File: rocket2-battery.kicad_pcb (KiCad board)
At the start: 4 copper layers, 91.4 x 69.8 mm, 141 parts, among them J1 Conn_01x07, J2 SMA, J3 ARM Cortex Debug, P1 PAD_SMD, P2 PAD_SMD, P3 PAD_SMD, P5 PAD_SMD, P6 PAD_SMD, P7 PAD_SMD, Q1 NMOS, Q2 NMOS, Q3 PMOS, Q4 PMOS, Q5 NMOS, Q6 NMOS, Q7 PMOS, Q8 PMOS, U1 3V3 LDO, Y1 16MHz

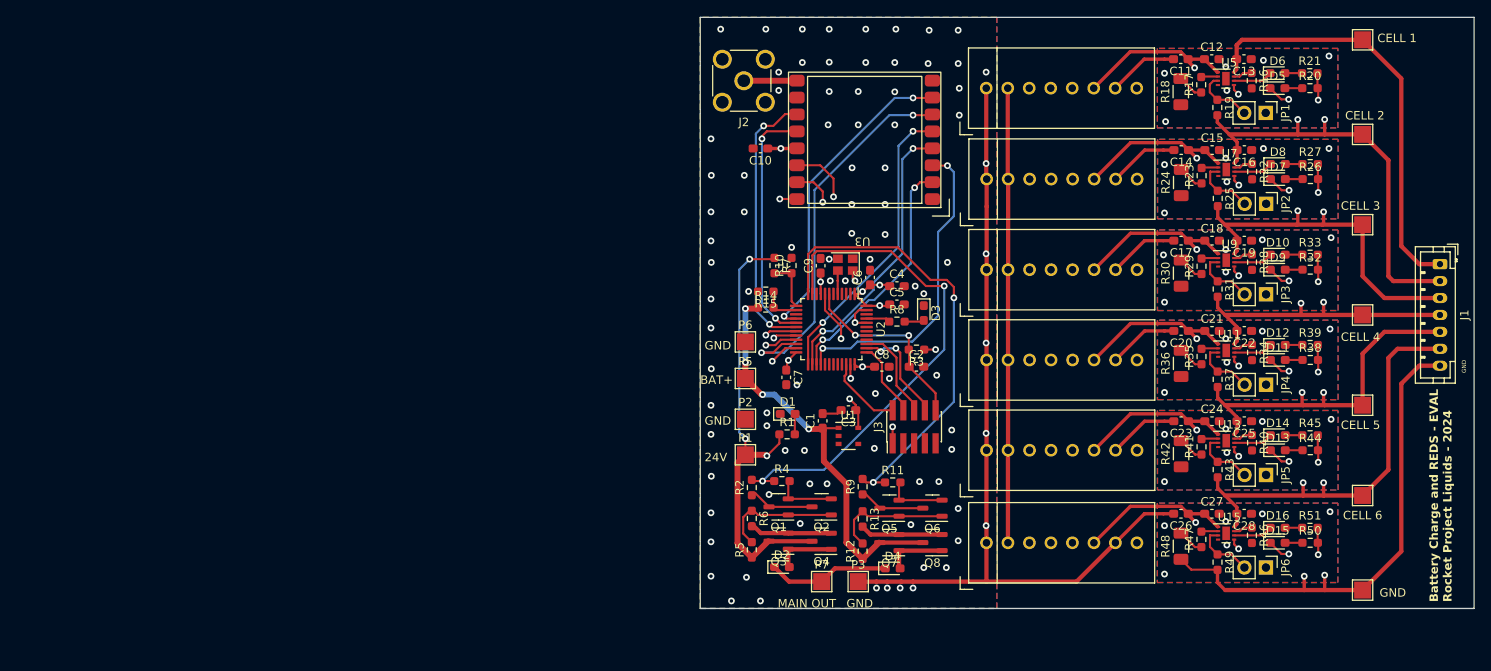
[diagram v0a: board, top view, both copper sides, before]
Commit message: Changed PMOS
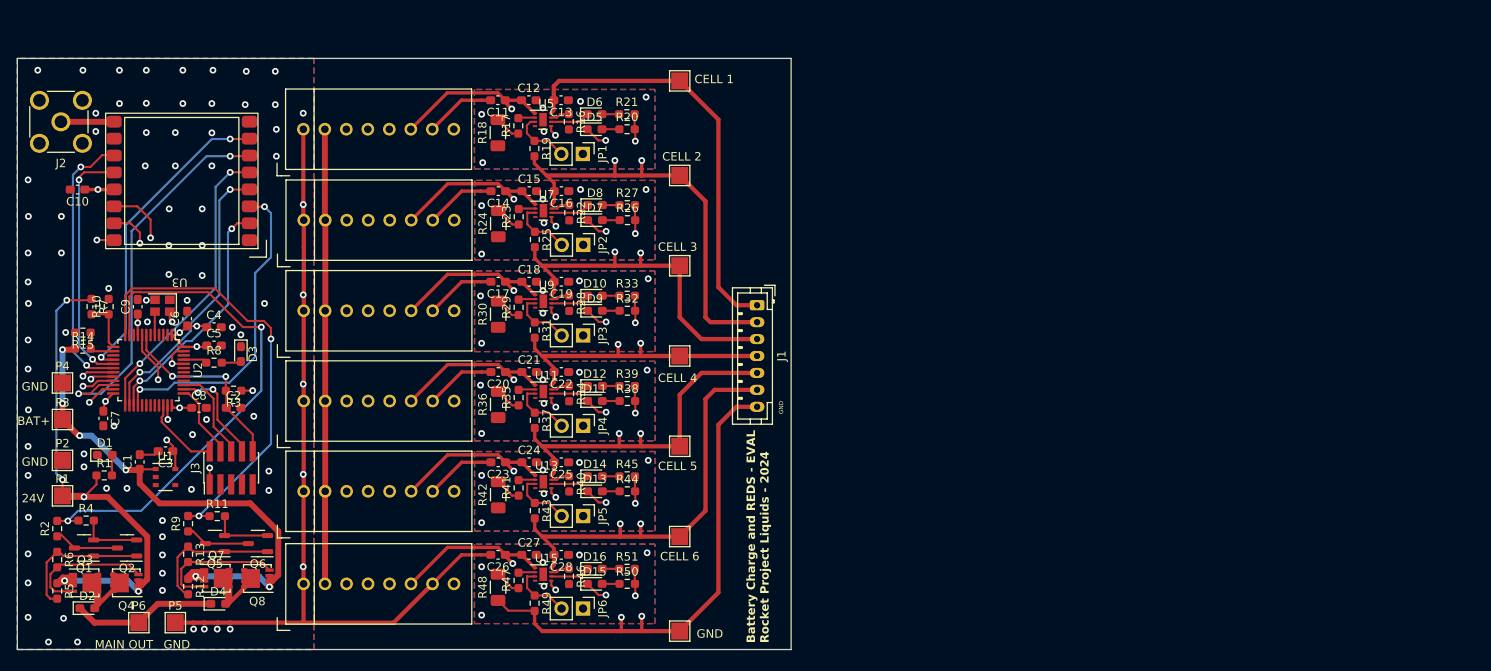
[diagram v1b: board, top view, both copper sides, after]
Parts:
- Q3, Q4, Q7, Q8: footprint Package_TO_SOT_SMD:SOT-23-3 -> Package_SO:Vishay_PowerPAK_1212-8_Single
- moved R4 82.4 mm to (111.6, 115.3)
- moved Q4 82.3 mm to (116.3, 122.7)
- moved D2 82.2 mm to (111.7, 125.7)
- moved Q2 82.2 mm to (116.4, 118.6)
- moved R2 82.2 mm to (108.2, 116.3)
- moved R5 82.2 mm to (108.2, 123.7), turned to -90 degrees
- moved R6 82.2 mm to (108.2, 120.0)
- moved Q1 82.2 mm to (111.3, 118.6)
- moved Q3 82.1 mm to (111.5, 122.7), turned to 0 degrees
- moved R21 80.8 mm to (175.5, 67.3)
- moved R27 80.8 mm to (175.5, 78.1)
- moved C10 80.8 mm to (110.6, 76.2)
- moved C11 80.8 mm to (160.2, 65.7)
- moved C12 80.8 mm to (163.9, 65.7)
- moved C13 80.8 mm to (167.7, 65.7)
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- renumbered P5 to P3, P6 to P4, P3 to P5, P7 to P6
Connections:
- Q3 pad 1: Net-(D2-A) -> +24V
- Q3 pad 2: Net-(Q3-G) -> +24V
- Q4 pad 1: Net-(D2-A) -> +24V
- Q4 pad 2: Net-(Q3-G) -> +24V
- Q7 pad 1: Net-(D4-A) -> /BATT_MAIN+
- Q7 pad 2: Net-(Q7-G) -> /BATT_MAIN+
- Q8 pad 1: Net-(D4-A) -> /BATT_MAIN+
- Q8 pad 2: Net-(Q7-G) -> /BATT_MAIN+
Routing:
- net /BATT_MAIN+: track 48.7 -> 65.6 mm, vias 4 -> 6
- net +24V: track 137.0 -> 149.2 mm, vias 3 -> 5
- net Net-(Q7-G): track 9.77 -> 15.8 mm
- net Net-(Q3-G): track 9.84 -> 15.8 mm
- net Net-(D2-A): track 7.24 -> 12.7 mm
- net Net-(D4-A): track 7.23 -> 12.6 mm
- net /MAIN+: track 15.0 -> 17.6 mm
- net Net-(Q1-D): track 14.0 -> 16.2 mm
- net Net-(Q5-D): track 14.3 -> 16.5 mm
- net MOSFET1: track 60.3 -> 61.5 mm
- net MOSFET2: track 54.0 -> 53.0 mm
- net GND: track 192.7 -> 192.6 mm, vias 102 -> 96

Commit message: some minor fixes
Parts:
- added D17: 30V 2A, Diode_SMD:D_0603_1608Metric_Pad1.05x0.95mm_HandSolder, F.Cu at (116.6, 109.1)
- added D18: 30V 2A, Diode_SMD:D_0603_1608Metric_Pad1.05x0.95mm_HandSolder, F.Cu at (117.5, 111.9)
- moved C1 0.89 mm to (118.5, 109.1)
- moved C3 0.89 mm to (121.5, 107.8)
- moved U1 0.89 mm to (121.5, 110.9)
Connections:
- C1 pad 1: /BATT_MAIN+ -> Net-(D17-K)
- U1 pad 1: /BATT_MAIN+ -> Net-(D17-K)
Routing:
- net Net-(D17-K): track 0.00 -> 5.80 mm
- net /BATT_MAIN+: track 65.6 -> 62.4 mm, vias 6 -> 7
- net +24V: track 149.2 -> 152.0 mm
- net GND: track 192.6 -> 190.9 mm, vias 96 -> 99
- net +3.3V: track 29.0 -> 27.3 mm

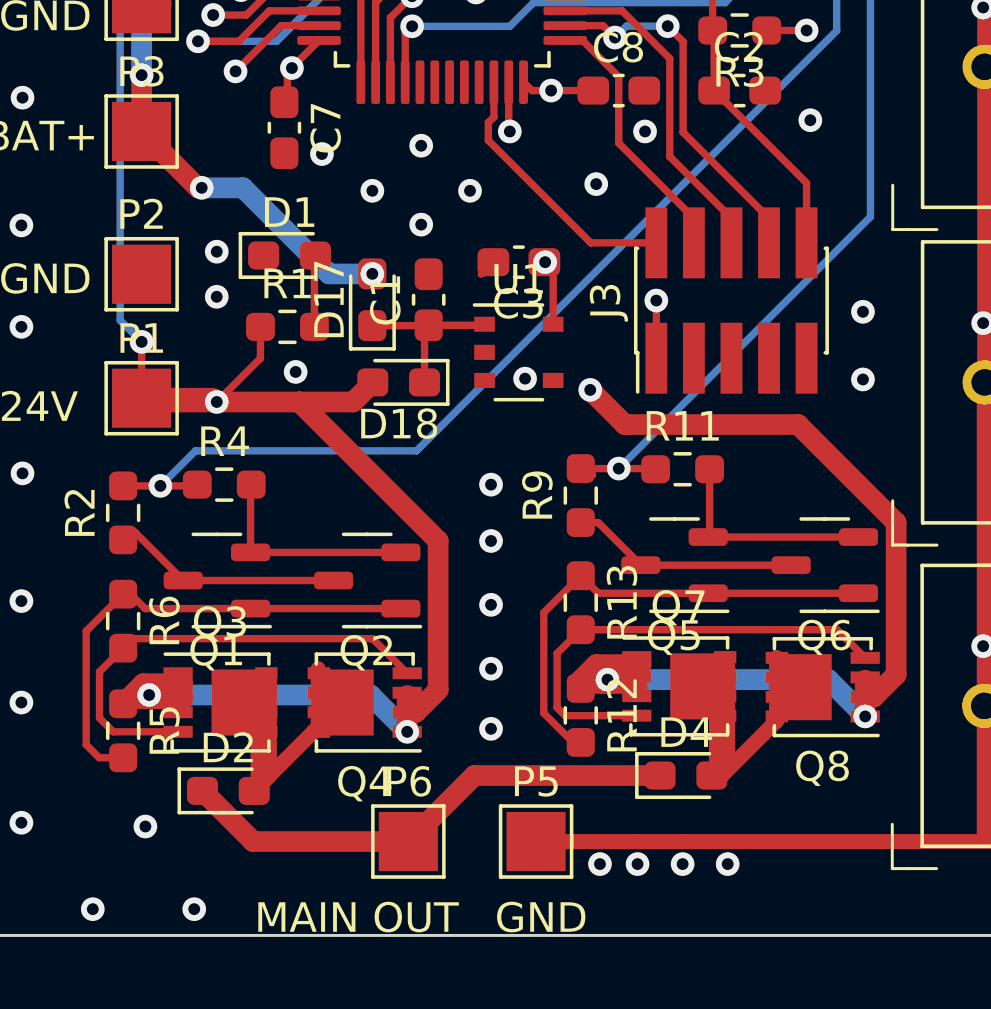
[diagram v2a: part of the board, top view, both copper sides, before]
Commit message: Fix diode footprints & other things I don't remember
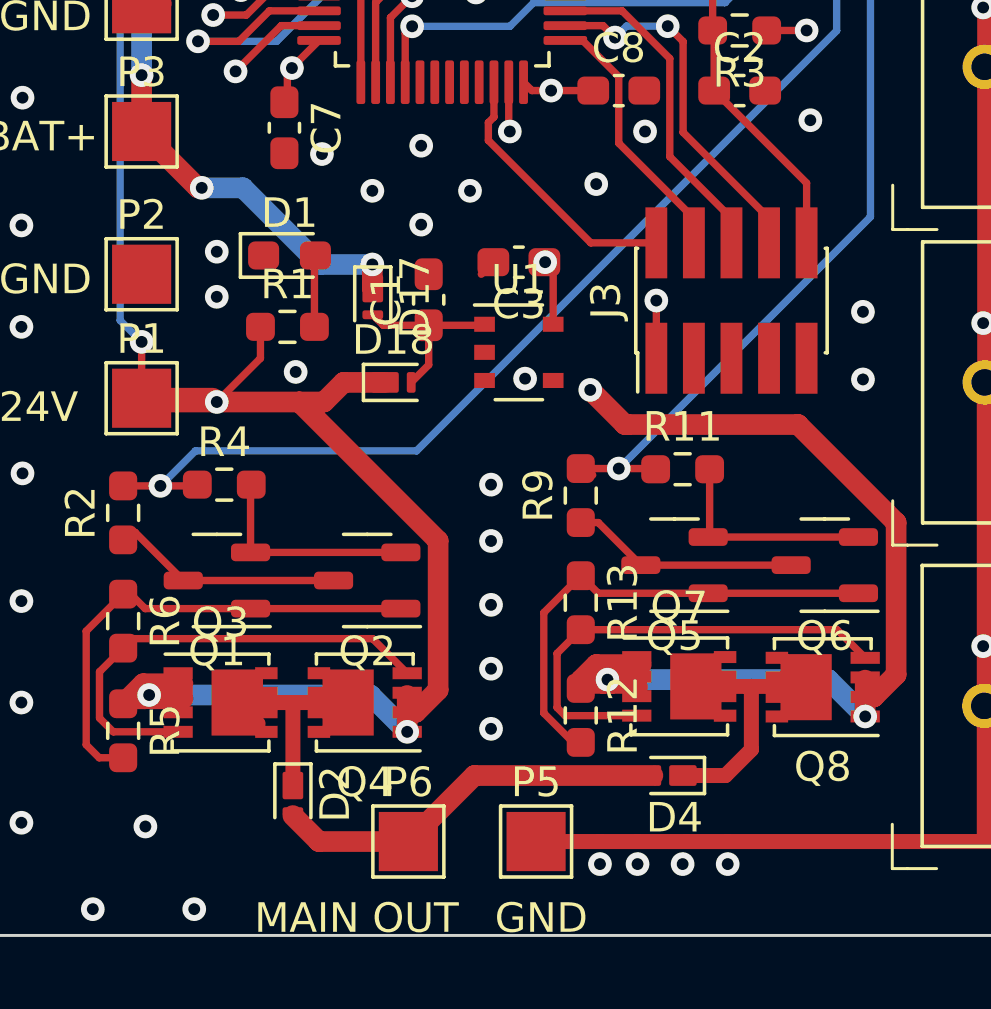
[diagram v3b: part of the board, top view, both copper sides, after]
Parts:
- D17, D18, D2, D4: footprint Diode_SMD:D_0603_1608Metric_Pad1.05x0.95mm_HandSolder -> Diode_SMD:Nexperia_DSN1608-2_1.6x0.8mm
- moved D2 2.18 mm to (113.9, 125.8), turned to -90 degrees
- moved D4 0.39 mm to (126.8, 125.2), turned to 180 degrees
- moved D18 0.17 mm to (117.3, 111.9), turned to 0 degrees
- moved D17 0.09 mm to (116.6, 109.0), turned to -90 degrees
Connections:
- D17 pad 1: Net-(D17-K) -> /BATT_MAIN+
- D17 pad 2: /BATT_MAIN+ -> Net-(D17-K)
- D18 pad 1: Net-(D17-K) -> +24V
- D18 pad 2: +24V -> Net-(D17-K)
- D2 pad 1: /MAIN+ -> Net-(D2-A)
- D2 pad 2: Net-(D2-A) -> /MAIN+
- D4 pad 1: /MAIN+ -> Net-(D4-A)
- D4 pad 2: Net-(D4-A) -> /MAIN+
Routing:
- net Net-(D2-A): track 12.7 -> 7.57 mm
- net /MAIN+: track 17.6 -> 13.5 mm
- net Net-(D4-A): track 12.6 -> 8.56 mm
- net /BATT_MAIN+: track 62.4 -> 63.2 mm
- net Net-(D17-K): track 5.80 -> 6.33 mm

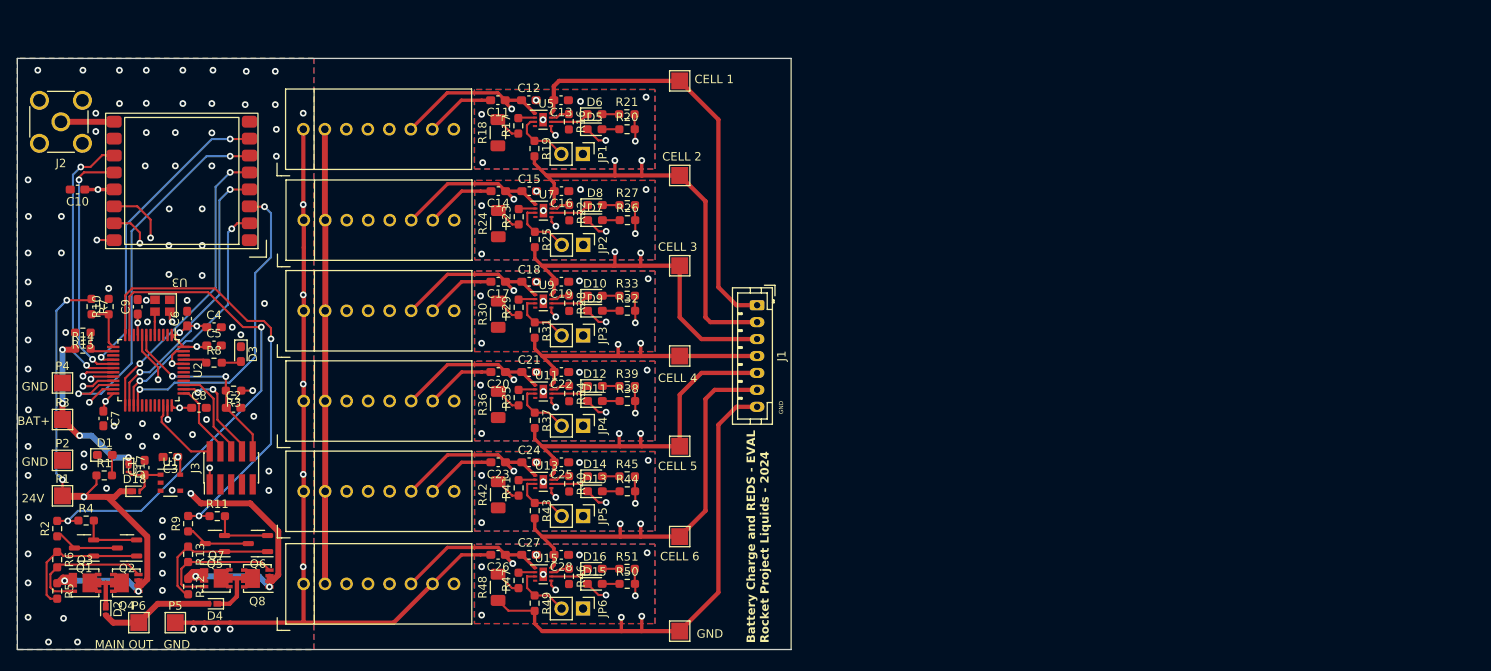
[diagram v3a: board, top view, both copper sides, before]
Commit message: fixed nmos
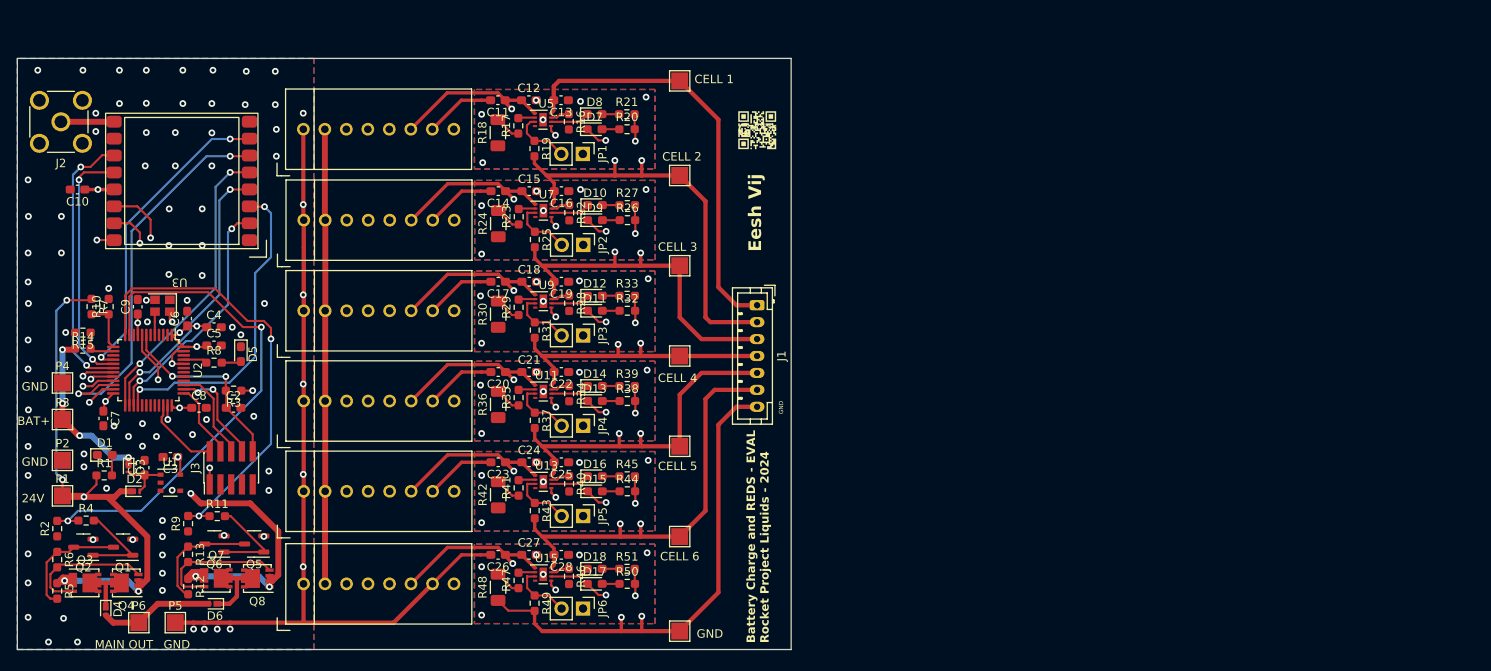
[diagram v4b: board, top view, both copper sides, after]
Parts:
- added G***: LOGO, LOGO, F.Cu at (190.9, 69.2)
- Q1, Q2, Q5, Q6: value NMOS -> Q_NMOS_GSD
- moved Q2 5.16 mm to (111.3, 118.5)
- moved Q6 5.14 mm to (126.7, 118.1)
- moved Q5 4.64 mm to (131.4, 118.1)
- moved Q1 4.62 mm to (116.0, 118.5)
- renumbered D8 to D10, D9 to D11, D10 to D12, D11 to D13, D12 to D14, D13 to D15, D14 to D16, D15 to D17, D16 to D18, D18 to D2, D17 to D3, D2 to D4, D3 to D5, D4 to D6, D5 to D7, D6 to D8, D7 to D9
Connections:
- Q1 pad 1: Net-(Q1-D) -> Net-(Q1-G)
- Q1 pad 2: Net-(Q1-G) -> GND
- Q1 pad 3: GND -> Net-(Q1-D)
- Q2 pad 1: Net-(Q1-D) -> Net-(Q1-G)
- Q2 pad 2: Net-(Q1-G) -> GND
- Q2 pad 3: GND -> Net-(Q1-D)
- Q5 pad 1: Net-(Q5-D) -> Net-(Q5-G)
- Q5 pad 2: Net-(Q5-G) -> GND
- Q5 pad 3: GND -> Net-(Q5-D)
- Q6 pad 1: Net-(Q5-D) -> Net-(Q5-G)
- Q6 pad 2: Net-(Q5-G) -> GND
- Q6 pad 3: GND -> Net-(Q5-D)
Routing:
- net GND: track 190.9 -> 175.9 mm, vias 99 -> 103
- net Net-(Q1-G): track 6.87 -> 11.3 mm
- net Net-(Q5-G): track 7.62 -> 11.5 mm
- net Net-(Q5-D): track 16.5 -> 13.6 mm
- net Net-(Q1-D): track 16.2 -> 13.9 mm
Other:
- board text added: "Eesh Vij"
